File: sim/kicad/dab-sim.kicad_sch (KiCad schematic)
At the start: 24 parts, among them T1 XFMR 8.33:1

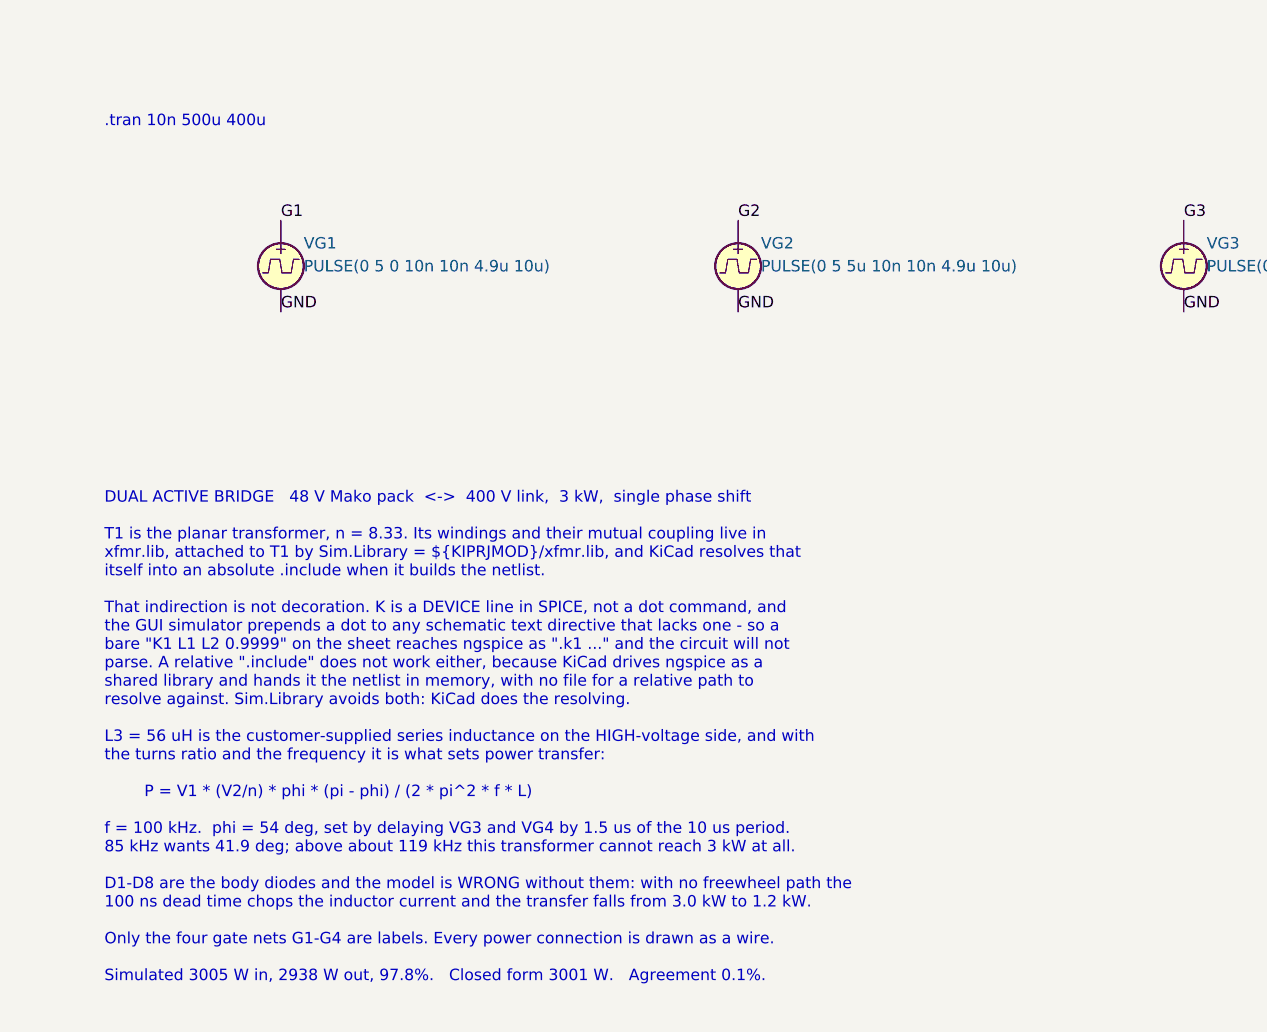
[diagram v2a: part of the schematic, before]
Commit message: Give every diode real parameters - ideal diodes were aborting the run
Reported: the circuit now parses and runs, but the transient aborts with
"Timestep too small ... trouble with __d4-instance d4" at 9.9 us.

Cause is mine. When I deleted and re-placed the diodes to fix their
rotation, the re-place wiped their Sim.Params and I only restored
Sim.Device and Sim.Pins. All eight were therefore running on ngspice
defaults - IS=1e-14, RS=0, CJO=0 - a perfectly ideal diode with no series
resistance and no junction capacitance, which in a hard-switching bridge
is a reliable way to stall the timestep. Verified from the exported
netlist: eight ".model __Dn D" lines with no parameters at all.

All eight now carry is/rs/n/cjo/tt/bv, and a .options line loosens abstol
from its 1 pA default, which is meaningless in a circuit carrying 60 A.

I cannot reproduce the failure here - ngspice 42 against 46, and the CLI
netlist has none of the probe instrumentation the GUI wraps every device
in - so this is the cause removed, not the fix observed. What is verified
is that the result is unchanged and stable, including under
ngbehavior=pslta, the compatibility mode KiCad selects: 3016 W in,
2943 W out, 97.6%, against the closed form's 3001 W. The small shift from
3005/2938 is the diodes now having a real forward drop, which is more
correct rather than less.

Co-Authored-By: Claude Opus 5 <noreply@anthropic.com>
Claude-Session: https://claude.ai/code/session_018xNdiSQv3JdagdWVUHe6u6
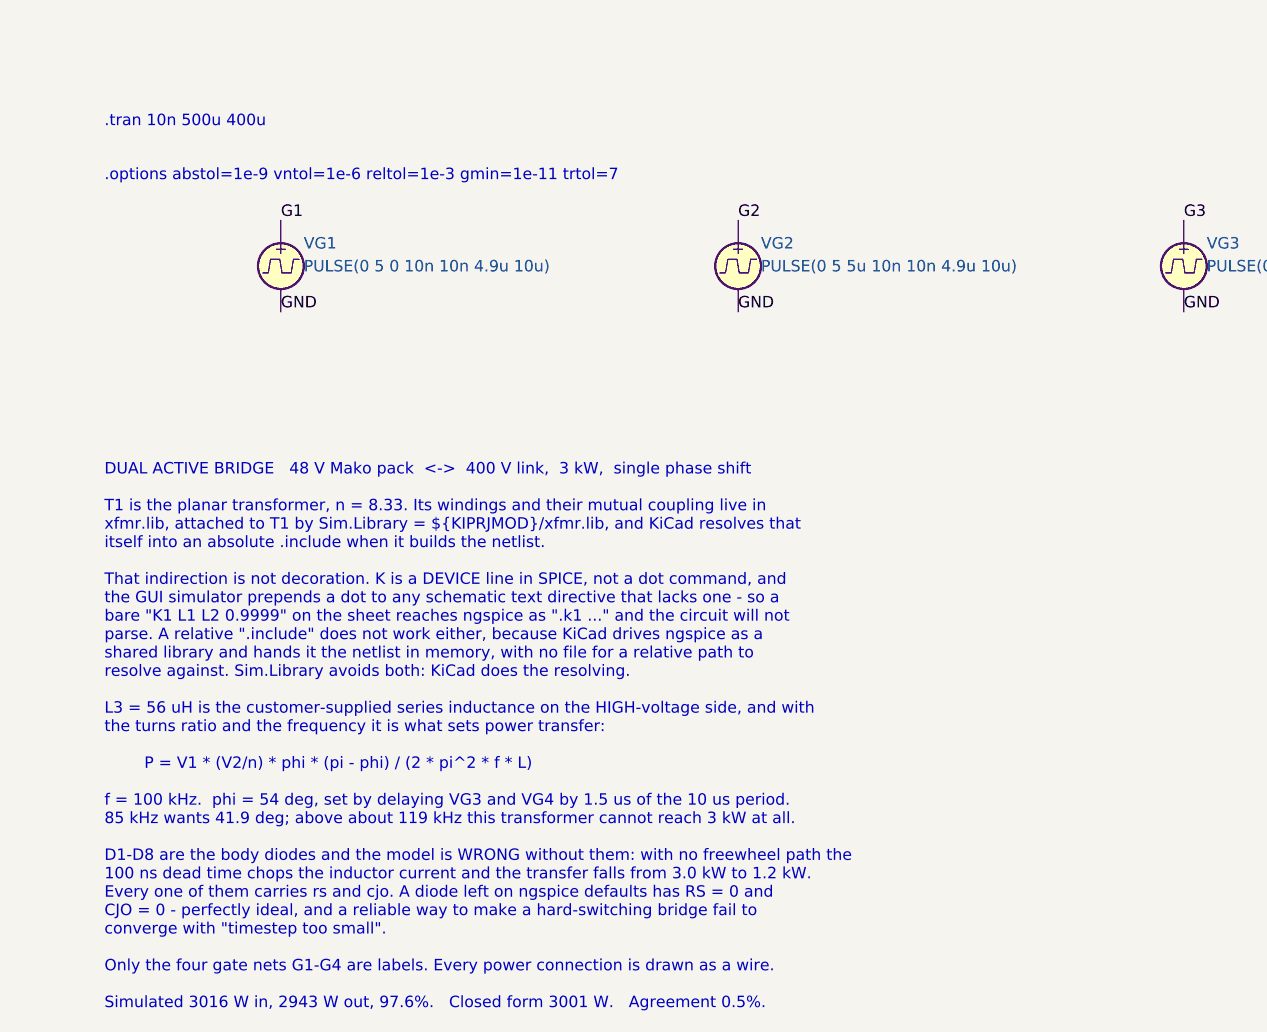
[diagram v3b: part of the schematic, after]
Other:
- note added: ".options abstol=1e-9 vntol=1e-6 reltol=1e-3 gmin=1e-11 trtol=7"
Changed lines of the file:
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@@
 		)
 	)
-  (text "DUAL ACTIVE BRIDGE   48 V Mako pack  <->  400 V link,  3 kW,  single phase shift\n\nT1 is the planar transformer, n = 8.33. Its windings and their mutual coupling live in\nxfmr.lib, attached to T1 by Sim.Library = ${KIPRJMOD}/xfmr.lib, and KiCad resolves that\nitself into an absolute .include when it builds the netlist.\n\nThat indirection is not decoration. K is a DEVICE line in SPICE, not a dot command, and\nthe GUI simulator prepends a dot to any schematic text directive that lacks one - so a\nbare \"K1 L1 L2 0.9999\" on the sheet reaches ngspice as \".k1 ...\" and the circuit will not\nparse. A relative \".include\" does not work either, because KiCad drives ngspice as a\nshared library and hands it the netlist in memory, with no file for a relative path to\nresolve against. Sim.Library avoids both: KiCad does the resolving.\n\nL3 = 56 uH is the customer-supplied series inductance on the HIGH-voltage side, and with\nthe turns ratio and the frequency it is what sets power transfer:\n\n        P = V1 * (V2/n) * phi * (pi - phi) / (2 * pi^2 * f * L)\n\nf = 100 kHz.  phi = 54 deg, set by delaying VG3 and VG4 by 1.5 us of the 10 us period.\n85 kHz wants 41.9 deg; above about 119 kHz this transformer cannot reach 3 kW at all.\n\nD1-D8 are the body diodes and the model is WRONG without them: with no freewheel path the\n100 ns dead time chops the inductor current and the transfer falls from 3.0 kW to 1.2 kW.\n\nOnly the four gate nets G1-G4 are labels. Every power connection is drawn as a wire.\n\nSimulated 3005 W in, 2938 W out, 97.8%.   Closed form 3001 W.   Agreement 0.1%."
-    (at 35 255 0)
+  (text ".options abstol=1e-9 vntol=1e-6 reltol=1e-3 gmin=1e-11 trtol=7"
+    (at 35 166 0)
     (effects (font (size 1.27 1.27)) (justify left bottom))
   )
+  (text "DUAL ACTIVE BRIDGE   48 V Mako pack  <->  400 V link,  3 kW,  single phase shift\n\nT1 is the planar transformer, n = 8.33. Its windings and their mutual coupling live in\nxfmr.lib, attached to T1 by Sim.Library = ${KIPRJMOD}/xfmr.lib, and KiCad resolves that\nitself into an absolute .include when it builds the netlist.\n\nThat indirection is not decoration. K is a DEVICE line in SPICE, not a dot command, and\nthe GUI simulator prepends a dot to any schematic text directive that lacks one - so a\nbare \"K1 L1 L2 0.9999\" on the sheet reaches ngspice as \".k1 ...\" and the circuit will not\nparse. A relative \".include\" does not work either, because KiCad drives ngspice as a\nshared library and hands it the netlist in memory, with no file for a relative path to\nresolve against. Sim.Library avoids both: KiCad does the resolving.\n\nL3 = 56 uH is the customer-supplied series inductance on the HIGH-voltage side, and with\nthe turns ratio and the frequency it is what sets power transfer:\n\n        P = V1 * (V2/n) * phi * (pi - phi) / (2 * pi^2 * f * L)\n\nf = 100 kHz.  phi = 54 deg, set by delaying VG3 and VG4 by 1.5 us of the 10 us period.\n85 kHz wants 41.9 deg; above about 119 kHz this transformer cannot reach 3 kW at all.\n\nD1-D8 are the body diodes and the model is WRONG without them: with no freewheel path the\n100 ns dead time chops the inductor current and the transfer falls from 3.0 kW to 1.2 kW.\nEvery one of them carries rs and cjo. A diode left on ngspice defaults has RS = 0 and\nCJO = 0 - perfectly ideal, and a reliable way to make a hard-switching bridge fail to\nconverge with \"timestep too small\".\n\nOnly the four gate nets G1-G4 are labels. Every power connection is drawn as a wire.\n\nSimulated 3016 W in, 2943 W out, 97.6%.   Closed form 3001 W.   Agreement 0.5%."
+    (at 35 258 0)
+    (effects (font (size 1.27 1.27)) (justify left bottom))
+  )
 	(symbol
 		(lib_id "Simulation_SPICE:VDC")
@@
 			)
 		)
-	)
+		(property "Sim.Params" "is=5e-9 rs=20m n=1.6 cjo=200p tt=30n bv=1200"
+			(at 69.85 80.01 0)
+			(hide yes)
+			(effects
+				(font
+					(size 1.27 1.27)
+				)
+			)
+		))
 	(symbol
 		(lib_id "Simulation_SPICE:D")
@@
 			)
 		)
-	)
+		(property "Sim.Params" "is=5e-9 rs=20m n=1.6 cjo=200p tt=30n bv=1200"
+			(at 69.85 119.38 0)
+			(hide yes)
+			(effects
+				(font
+					(size 1.27 1.27)
+				)
+			)
+		))
 	(symbol
 		(lib_id "Simulation_SPICE:D")
@@
 			)
 		)
-	)
+		(property "Sim.Params" "is=5e-9 rs=20m n=1.6 cjo=200p tt=30n bv=1200"
+			(at 119.38 80.01 0)
+			(hide yes)
+			(effects
+				(font
+					(size 1.27 1.27)
+				)
+			)
+		))
 	(symbol
 		(lib_id "Simulation_SPICE:D")
@@
 			)
 		)
-	)
+		(property "Sim.Params" "is=5e-9 rs=20m n=1.6 cjo=200p tt=30n bv=1200"
+			(at 119.38 119.38 0)
+			(hide yes)
+			(effects
+				(font
+					(size 1.27 1.27)
+				)
+			)
+		))
 	(symbol
 		(lib_id "Simulation_SPICE:D")
@@
 			)
 		)
-	)
+		(property "Sim.Params" "is=5e-9 rs=20m n=1.6 cjo=200p tt=30n bv=1200"
+			(at 199.39 80.01 0)
+			(hide yes)
+			(effects
+				(font
+					(size 1.27 1.27)
+				)
+			)
+		))
 	(symbol
 		(lib_id "Simulation_SPICE:D")
@@
 			)
 		)
-	)
+		(property "Sim.Params" "is=5e-9 rs=20m n=1.6 cjo=200p tt=30n bv=1200"
+			(at 199.39 119.38 0)
+			(hide yes)
+			(effects
+				(font
+					(size 1.27 1.27)
+				)
+			)
+		))
 	(symbol
 		(lib_id "Simulation_SPICE:D")
@@
 			)
 		)
-	)
+		(property "Sim.Params" "is=5e-9 rs=20m n=1.6 cjo=200p tt=30n bv=1200"
+			(at 250.19 80.01 0)
+			(hide yes)
+			(effects
+				(font
+					(size 1.27 1.27)
+				)
+			)
+		))
 	(symbol
 		(lib_id "Simulation_SPICE:D")
@@
 			)
 		)
-	)
+		(property "Sim.Params" "is=5e-9 rs=20m n=1.6 cjo=200p tt=30n bv=1200"
+			(at 250.19 119.38 0)
+			(hide yes)
+			(effects
+				(font
+					(size 1.27 1.27)
+				)
+			)
+		))
 	(symbol
 		(lib_id "power:GND")
